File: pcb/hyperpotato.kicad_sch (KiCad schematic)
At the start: 44 parts, among them J1 Conn_01x02_Socket, J2 Conn_01x03_Pin, J3 Conn_01x05_Socket, Q1 AO3401A, SW1 SW_Push_45deg, SW10 SW_Push_45deg, SW11 SW_Push_45deg, SW12 SW_Push_45deg, SW13 SW_Push_45deg, SW14 SW_SPDT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

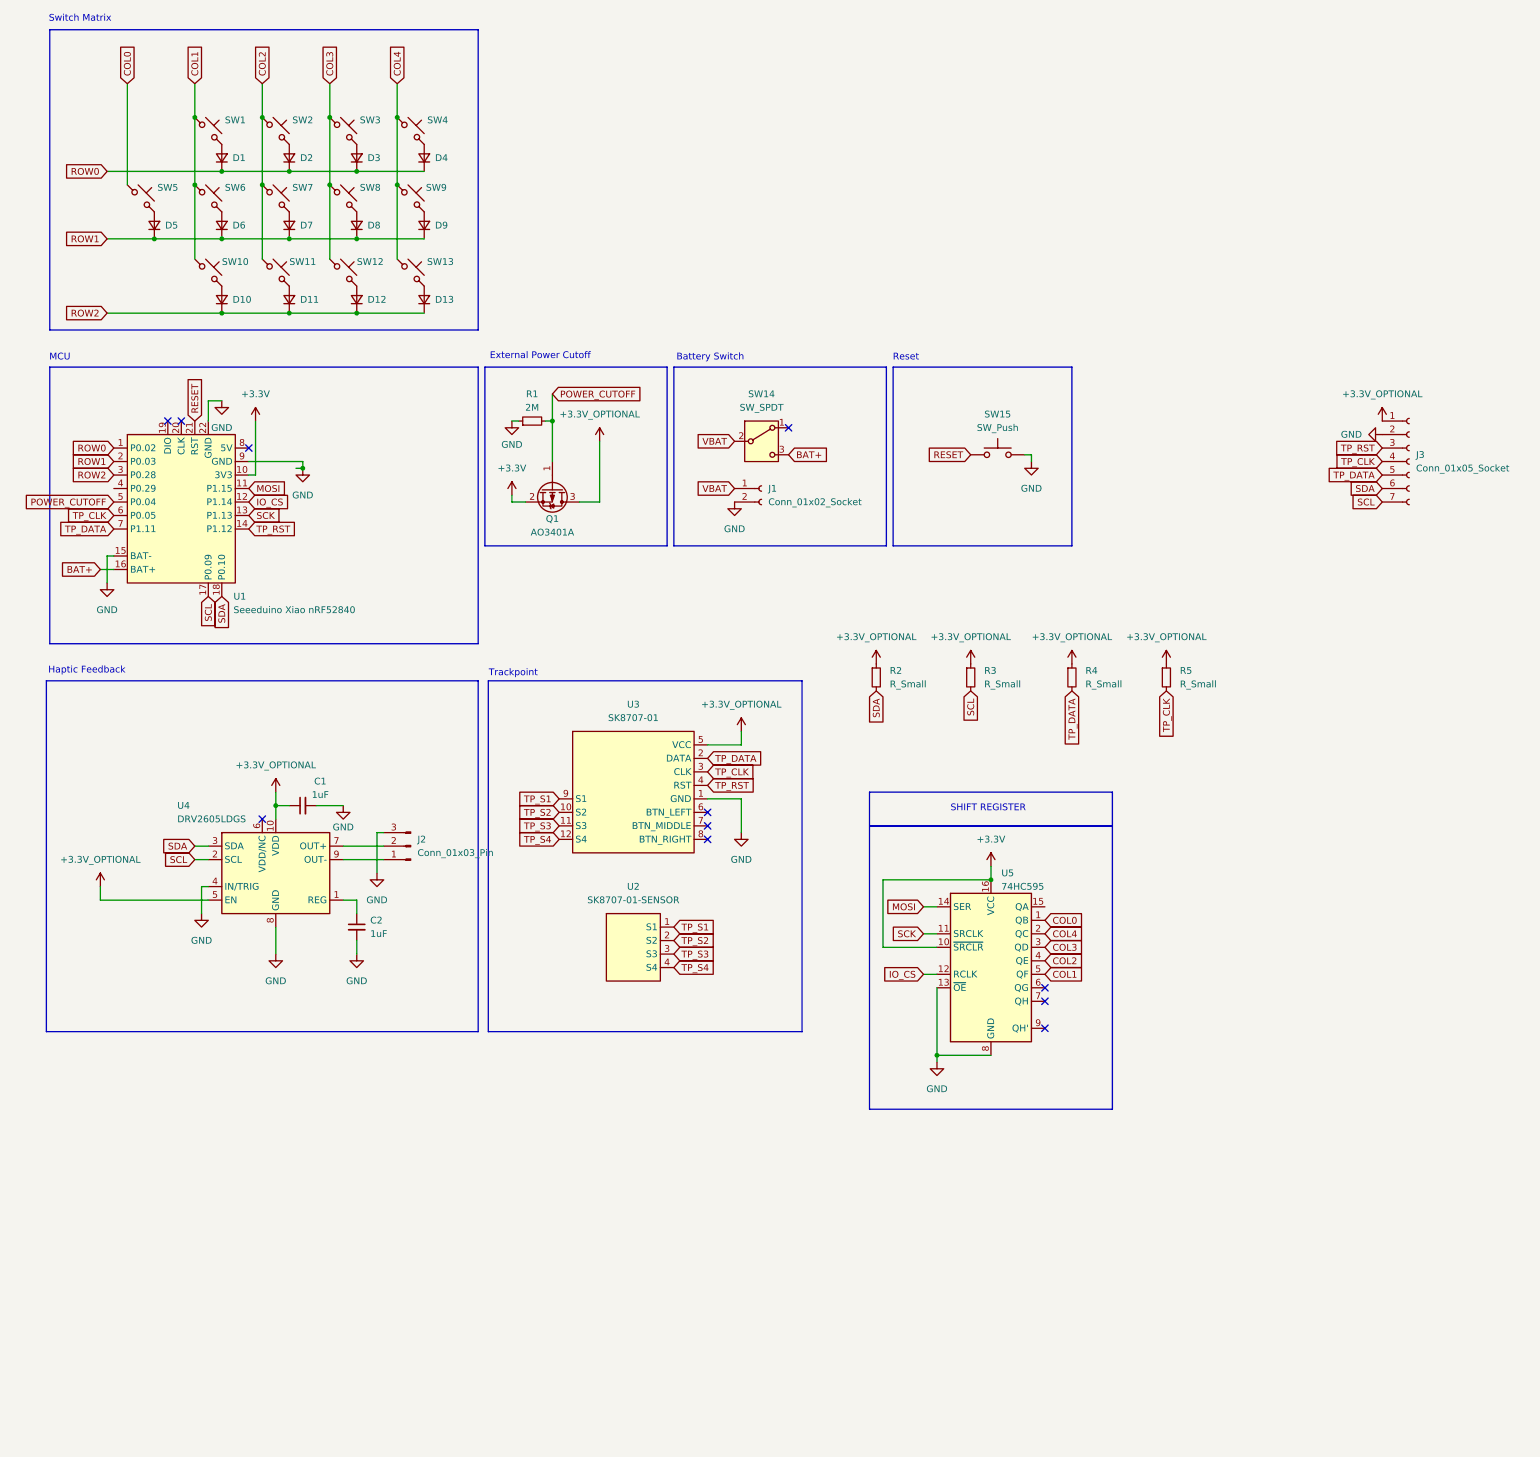
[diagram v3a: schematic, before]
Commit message: Basic routing and diodes routing
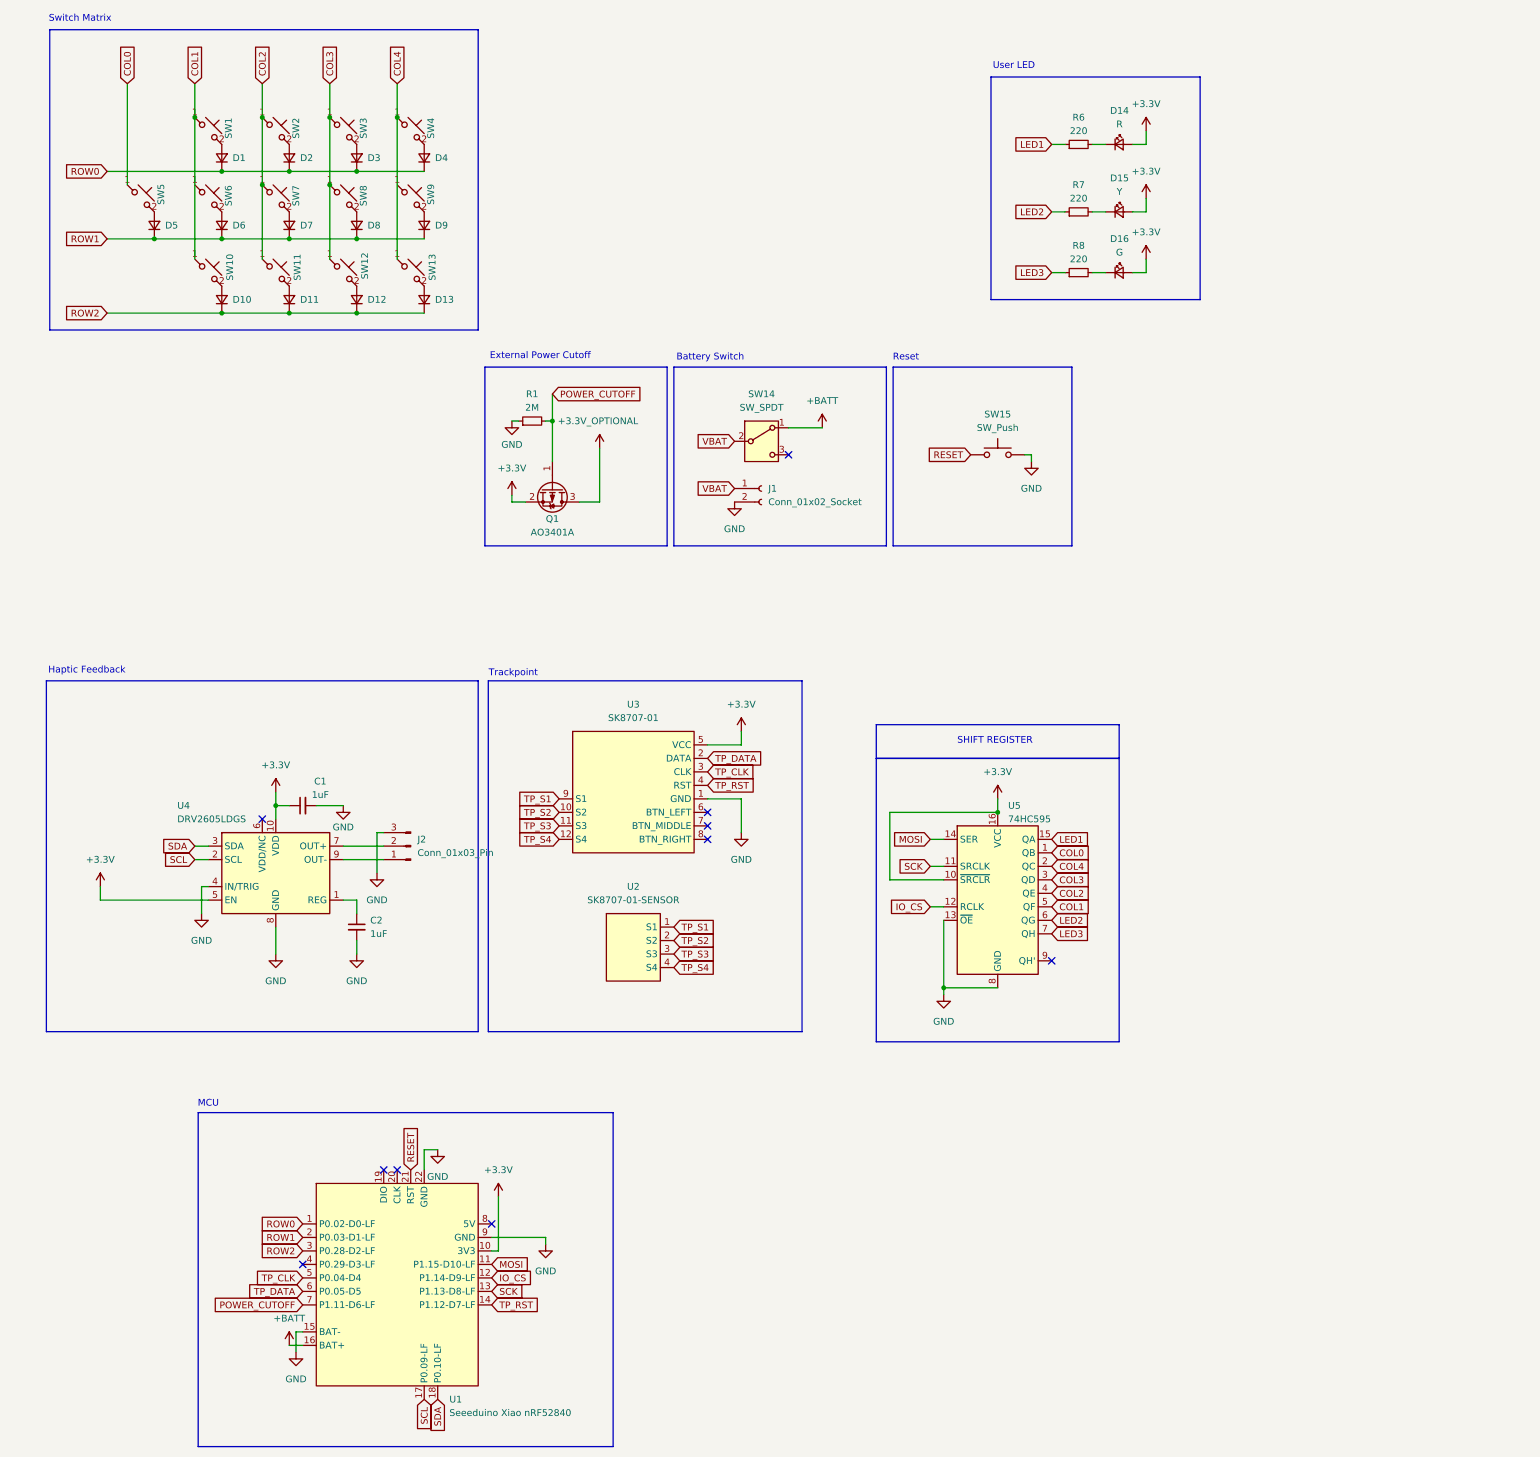
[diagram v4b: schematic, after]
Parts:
- removed J3: Conn_01x05_Socket, Connector_PinHeader_2.54mm:PinHeader_1x07_P2.54mm_Vertical, symbol Connector:Conn_01x07_Socket
- removed R2, R3, R4, R5: R_Small, ssbb_parts:R_0603_1608Metric_reversible, symbol Device:R_Small
- added D14: R, LED_THT:LED_D3.0mm, symbol Device:LED_Small
- added D15: Y, LED_THT:LED_D3.0mm, symbol Device:LED_Small
- added D16: G, LED_THT:LED_D3.0mm, symbol Device:LED_Small
- added R6, R7, R8: 220, ssbb_parts_reversible:R_1206_3216Metric_reversible, symbol Device:R_Small
- C1, C2: footprint ssbb_parts:C_0603_1608Metric_reversible -> ssbb_parts_reversible:C_1206_3216Metric_reversible
- D1, D10, D11, D12, D13, D2, D3, D4, D5, D6, D7, D8, D9: footprint Diode_SMD:D_1206_3216Metric -> ssbb_parts_reversible:D_1206_3216Metric_reversible
- J1: footprint ssbb_parts:Molex_Pico-EZmate_78171-0002_1x02-1MP_P1.20mm_Vertical_reversible -> ssbb_parts_reversible:Molex_Pico-EZmate_78171-0002_1x02-1MP_P1.20mm_Vertical_reversible
- Q1: footprint ssbb_parts:SOT-23_reversible -> Package_TO_SOT_SMD:SOT-23
- R1: footprint ssbb_parts:R_0603_1608Metric_reversible -> ssbb_parts_reversible:R_1206_3216Metric_reversible
- SW14: footprint ssbb_parts:SW_SPDT_PCM12_reversible -> ssbb_parts_reversible:SW_SPDT_PCM12_reversible
- SW15: footprint ssbb_parts:Panasonic_EVQPUL_EVQPUC_reversible -> ssbb_parts:SW_SPST_SKQG_WithStem_reversible
- U1: symbol PCM_marbastlib-promicroish:Seeeduino_Xiao_nRF52840 -> ssbb_parts:Seeeduino_Xiao_nRF52840
- U2: footprint ssbb_parts:Sprintek_SK8707-01_Sensor_reversible -> ssbb_parts:TP_Lenovo_T460S_Sensor
- U3: footprint ssbb_parts:Sprintek_SK8707-01_reversible -> ssbb_parts:TP_Sprintek_SK8707-01_reversible
- U4: footprint ssbb_parts:VSSOP-10_3x3mm_P0.5mm_reversible -> ssbb_parts_reversible:VSSOP-10_3x3mm_P0.5mm_reversible
- U5: footprint ssbb_parts:TSSOP-16_4.4x5mm_P0.65mm_reversible -> ssbb_parts_reversible:SOIC-16_3.9x9.9mm_P1.27mm_reversible
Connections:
- net +3.3V: now also C1.1, U3.5 (VCC), U4.10 (VDD), U4.5 (EN), D14.2 (A), D15.2 (A), D16.2 (A)
- net +3.3V_OPTIONAL: no longer C1.1, U3.5 (VCC), U4.10 (VDD), U4.5 (EN)
- net COL1: no longer SW6.1
- net COL4: now also SW4.1; no longer SW4.2, SW9.2
- net POWER_CUTOFF: now also U1.7 (P1.11-D6-LF); no longer U1.5 (P0.04)
- net TP_CLK: now also U1.5 (P0.04-D4); no longer U1.6 (P0.05)
- net TP_DATA: now also U1.6 (P0.05-D5); no longer U1.7 (P1.11)
- net at D9.2 (A): now also SW9.2; no longer SW9.1
- net at D4.2 (A): now also SW4.2; no longer SW4.1
- net +BATT: now reaches SW14.1 (A)
- net +BATT: now also U1.16 (BAT+)
- net LED1: now reaches U5.15 (QA)
- net LED1: now also R6.1
- net LED2: now reaches U5.6 (QG)
- net LED2: now also R7.1
- net LED3: now reaches U5.7 (QH)
- net LED3: now also R8.1
- net BAT+: no longer names the net of SW14.3 (C)
- net BAT+: no longer U1.16 (BAT+)
- new net: D14.1 (K), R6.2
- new net: D15.1 (K), R7.2
- new net: D16.1 (K), R8.2
- no-connect marks 11 -> 10
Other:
- note added: "User LED"
- moved on the sheet: U1, U5

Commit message: Good progsess on tracks
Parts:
- added H1: MountingHole, ssbb_parts:TP_Lenovo_T460S_Sensor, symbol Mechanical:MountingHole
- U2: footprint ssbb_parts:TP_Lenovo_T460S_Sensor -> ssbb_parts:TP_Sensor_Connector_reversible
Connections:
- net COL1: now also SW6.1
- net COL4: now also SW9.1
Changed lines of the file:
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@@
 	)
 	(junction
+		(at 81.28 46.99)
+		(diameter 0)
+		(color 0 0 0 0)
+	)
+	(junction
 		(at 48.26 71.12)
 		(diameter 0)
@@
 	)
 	(junction
+		(at 43.18 46.99)
+		(diameter 0)
+		(color 0 0 0 0)
+	)
+	(junction
 		(at 110.49 91.44)
 		(diameter 0)
@@
 	(wire
 		(pts
+			(xy 81.28 46.99) (xy 81.28 60.96)
+		)
+		(stroke
+			(width 0)
+			(type default)
+		)
+	)
+	(wire
+		(pts
 			(xy 184.15 185.42) (xy 184.15 198.12)
 		)
@@
 	(wire
 		(pts
-			(xy 43.18 34.29) (xy 43.18 60.96)
+			(xy 43.18 34.29) (xy 43.18 46.99)
 		)
 		(stroke
@@
 	(wire
 		(pts
-			(xy 25.4 179.07) (xy 25.4 181.61)
+			(xy 81.28 34.29) (xy 81.28 46.99)
 		)
 		(stroke
@@
 	(wire
 		(pts
-			(xy 100.33 237.49) (xy 100.33 247.65)
+			(xy 25.4 179.07) (xy 25.4 181.61)
 		)
 		(stroke
@@
 	(wire
 		(pts
-			(xy 139.7 162.56) (xy 146.05 162.56)
+			(xy 100.33 237.49) (xy 100.33 247.65)
 		)
 		(stroke
@@
 	(wire
 		(pts
-			(xy 43.18 27.94) (xy 43.18 34.29)
+			(xy 139.7 162.56) (xy 146.05 162.56)
 		)
 		(stroke
@@
 	(wire
 		(pts
-			(xy 154.94 92.71) (xy 161.29 92.71)
+			(xy 43.18 27.94) (xy 43.18 34.29)
 		)
 		(stroke
@@
 	(wire
 		(pts
-			(xy 200.66 97.79) (xy 200.66 99.06)
+			(xy 154.94 92.71) (xy 161.29 92.71)
 		)
 		(stroke
@@
 	(wire
 		(pts
-			(xy 81.28 34.29) (xy 81.28 60.96)
+			(xy 200.66 97.79) (xy 200.66 99.06)
 		)
 		(stroke
@@
 	(wire
 		(pts
+			(xy 43.18 46.99) (xy 43.18 60.96)
+		)
+		(stroke
+			(width 0)
+			(type default)
+		)
+	)
+	(wire
+		(pts
 			(xy 48.26 57.15) (xy 60.96 57.15)
 		)
@@
 			)
 		)
-		(property "Footprint" "ssbb_parts:TP_Lenovo_T460S_Sensor"
+		(property "Footprint" "ssbb_parts:TP_Sensor_Connector_reversible"
 			(at 125.73 190.5 0)
 			(effects
@@
 					(unit 1)
 				)
+			)
+		)
+	)
+	(symbol
+		(lib_id "Mechanical:MountingHole")
+		(at 105.41 186.69 0)
+		(unit 1)
+		(exclude_from_sim yes)
+		(in_bom no)
+		(on_board yes)
+		(dnp no)
+		(fields_autoplaced yes)
+		(property "Reference" "H1"
+			(at 107.95 185.42 0)
+			(effects
+				(font
+					(size 1.27 1.27)
+				)
+				(justify left)
+			)
+		)
+		(property "Value" "MountingHole"
+			(at 107.95 187.96 0)
+			(effects
+				(font
+					(size 1.27 1.27)
+				)
+				(justify left)
+			)
+		)
+		(property "Footprint" "ssbb_parts:TP_Lenovo_T460S_Sensor"
+			(at 105.41 186.69 0)
+			(effects
+				(font
+					(size 1.27 1.27)
+				)
+				(hide yes)
+			)
+		)
+		(property "Datasheet" "~"
+			(at 105.41 186.69 0)
+			(effects
+				(font
+					(size 1.27 1.27)
+				)
+				(hide yes)
+			)
+		)
+		(property "Description" "Mounting Hole without connection"
+			(at 105.41 186.69 0)
+			(effects
+				(font
+					(size 1.27 1.27)
+				)
+				(hide yes)
+			)
+		)
+		(instances
+			(project ""
+				(path "/19b5f7b9-14b9-4ffe-8621-f024a09d5ec4"
+					(reference "H1")
+					(unit 1)
+				)
